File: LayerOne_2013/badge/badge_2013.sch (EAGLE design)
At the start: 122 parts, among them CON2 EXT, CON6 J8, CON8 J3, IC1 SLICE_NOSHIFT_TLC5947HTSSOP32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, IC3 SLICE_NOSHIFT_TLC5947HTSSOP32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, IC4 TL064D, K1 5-XX, K2 5-XX, K3 5-XX, K4 5-XX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

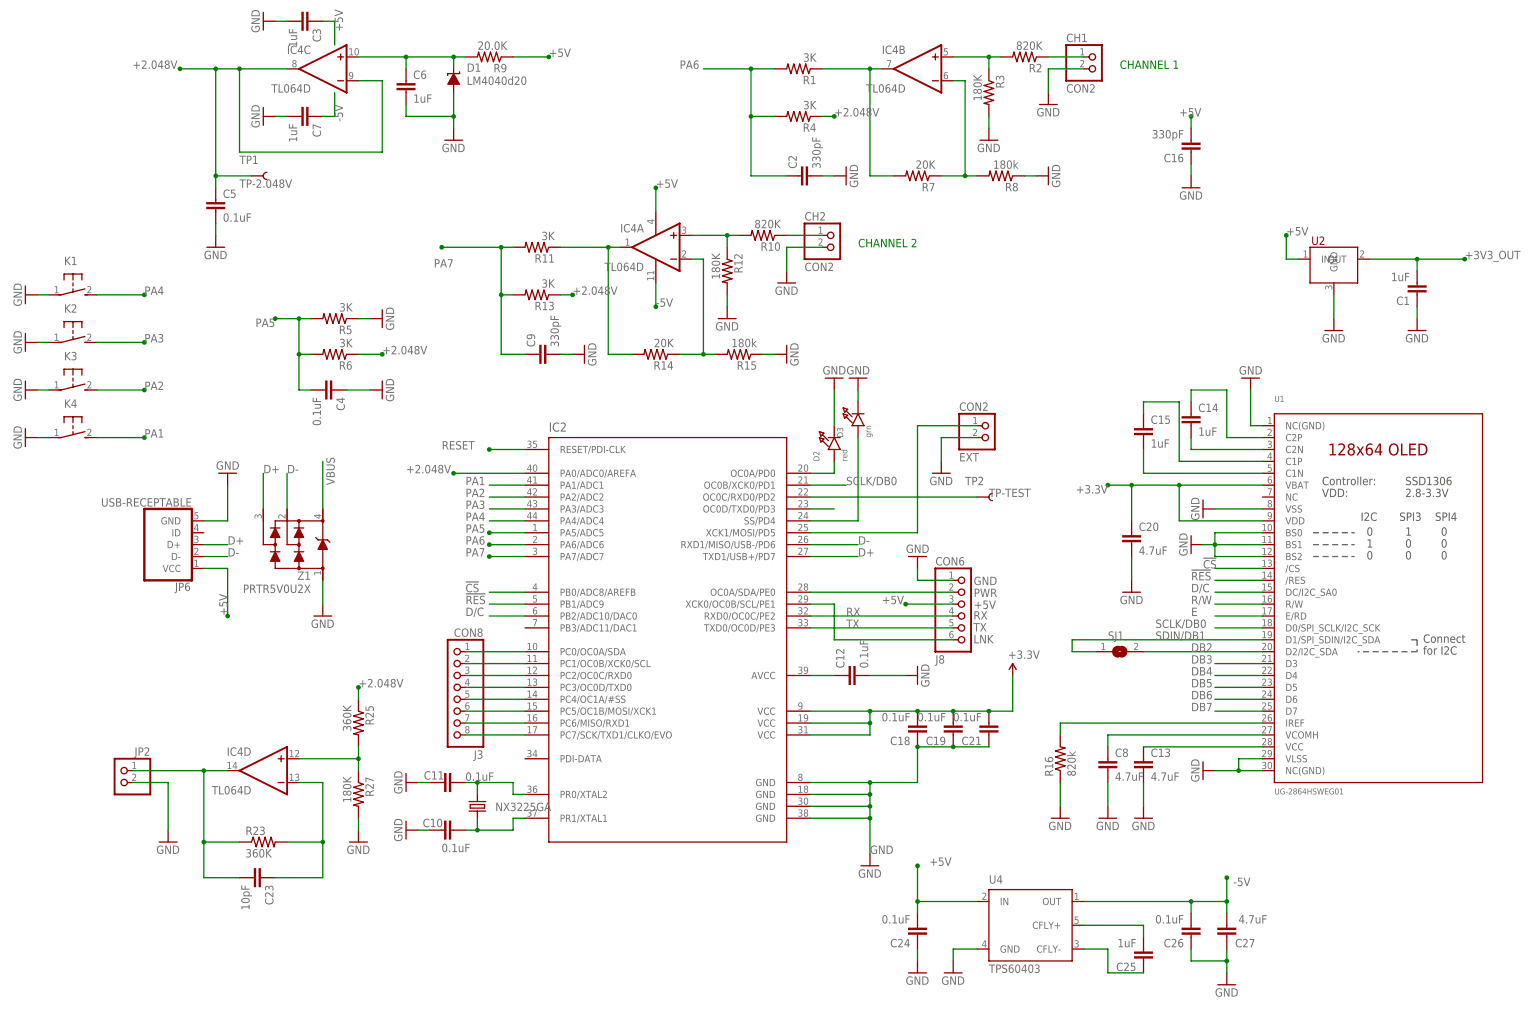
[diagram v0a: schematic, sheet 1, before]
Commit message: 
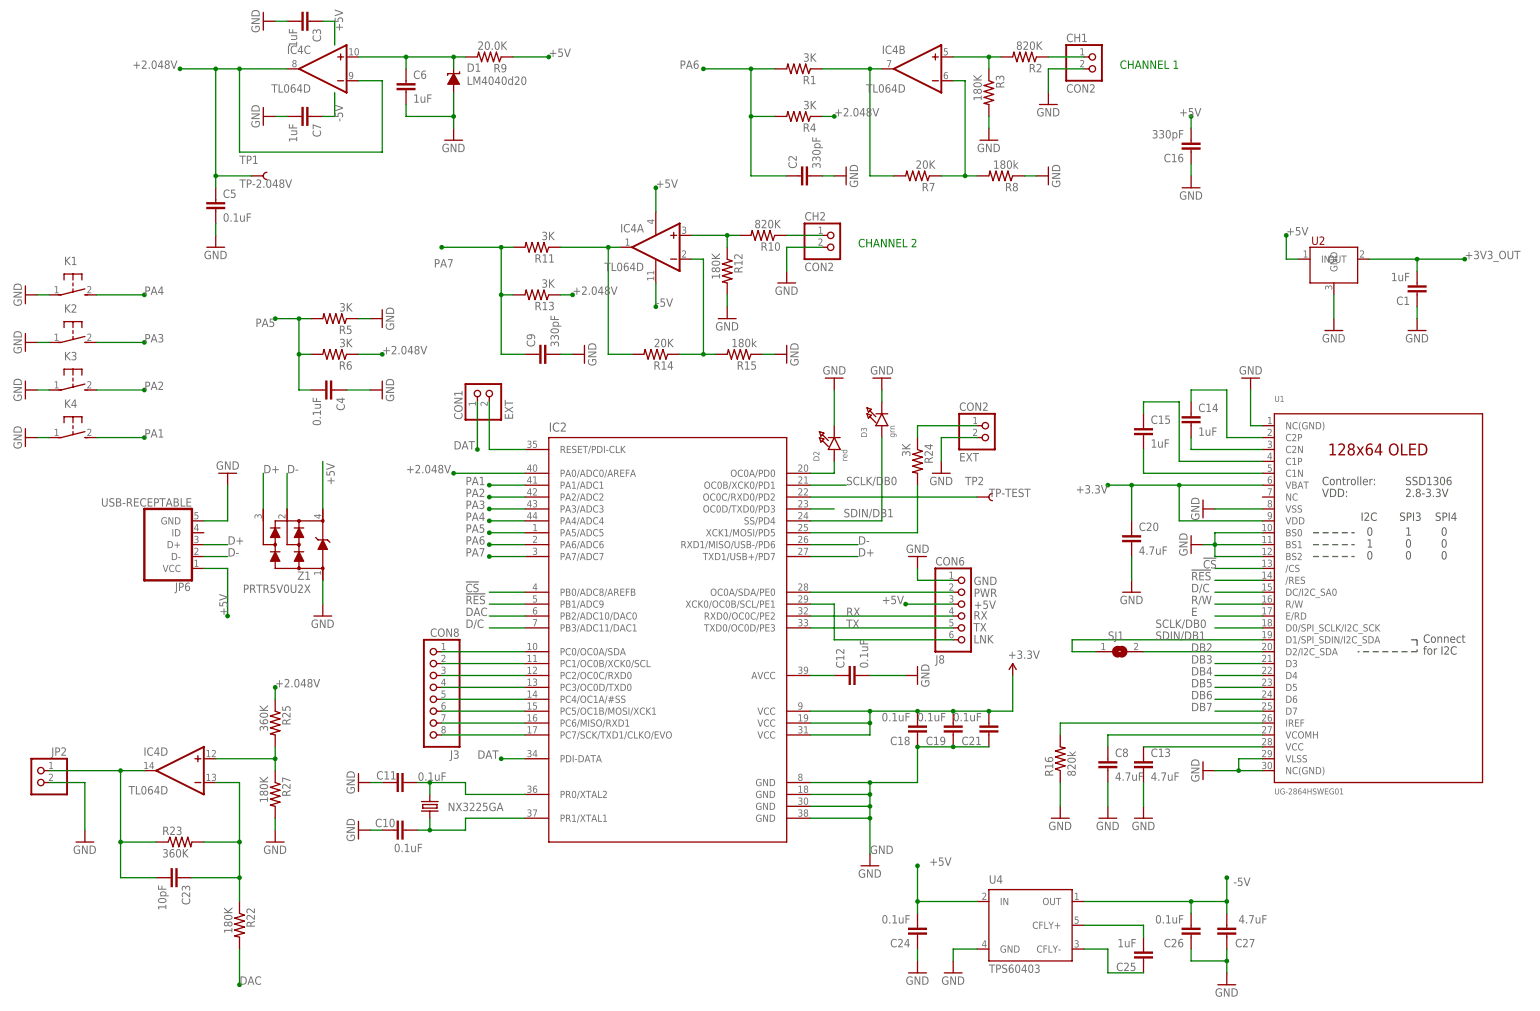
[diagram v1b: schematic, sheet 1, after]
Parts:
- added CON1: EXT, microbuilder:HEADER-1X2
- added R22: 180K, resistor:R-US_R0805
- added R24: 3K, resistor:R-US_R0805
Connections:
- removed net RESET: IC2.RESET/PDI-CLK
- removed net VBUS: Z1.P$4
- new net DAC: IC2.PB2/ADC10/DAC0, R22.2
- new net DAT: CON1.1, IC2.PDI-DATA
- new net N$38: CON1.2, IC2.RESET/PDI-CLK
- new net N$6: CON2.1, R24.1
- net +5V: now also Z1.P$4
- net D/C: now also IC2.PB3/ADC11/DAC1; no longer IC2.PB2/ADC10/DAC0
- net N$19: now also R24.2; no longer CON2.1
- net N$24: now also R22.1
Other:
- moved on the sheet: C10, C11, C23, CON8, D3, IC4D, JP2, R23, R25, R27

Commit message: 
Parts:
- PDI: value EXT -> CON6
- renumbered CON1 to PDI
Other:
- moved on the sheet: C4, K1, K2, K3, K4, R5, R6

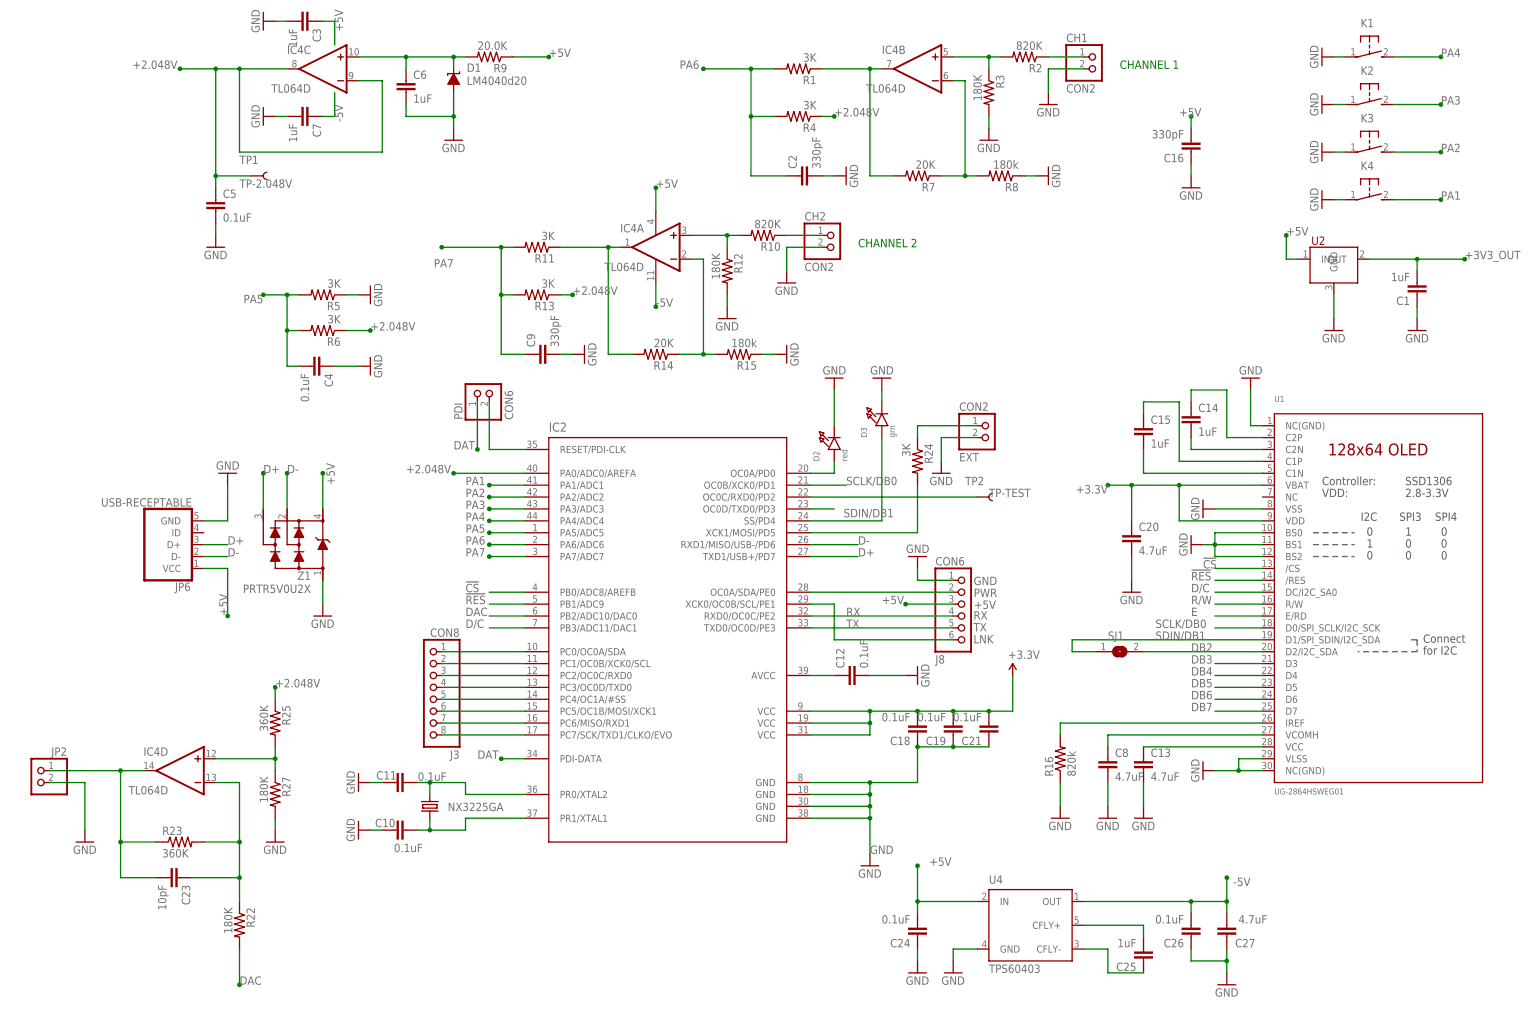
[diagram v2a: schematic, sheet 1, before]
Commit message: 
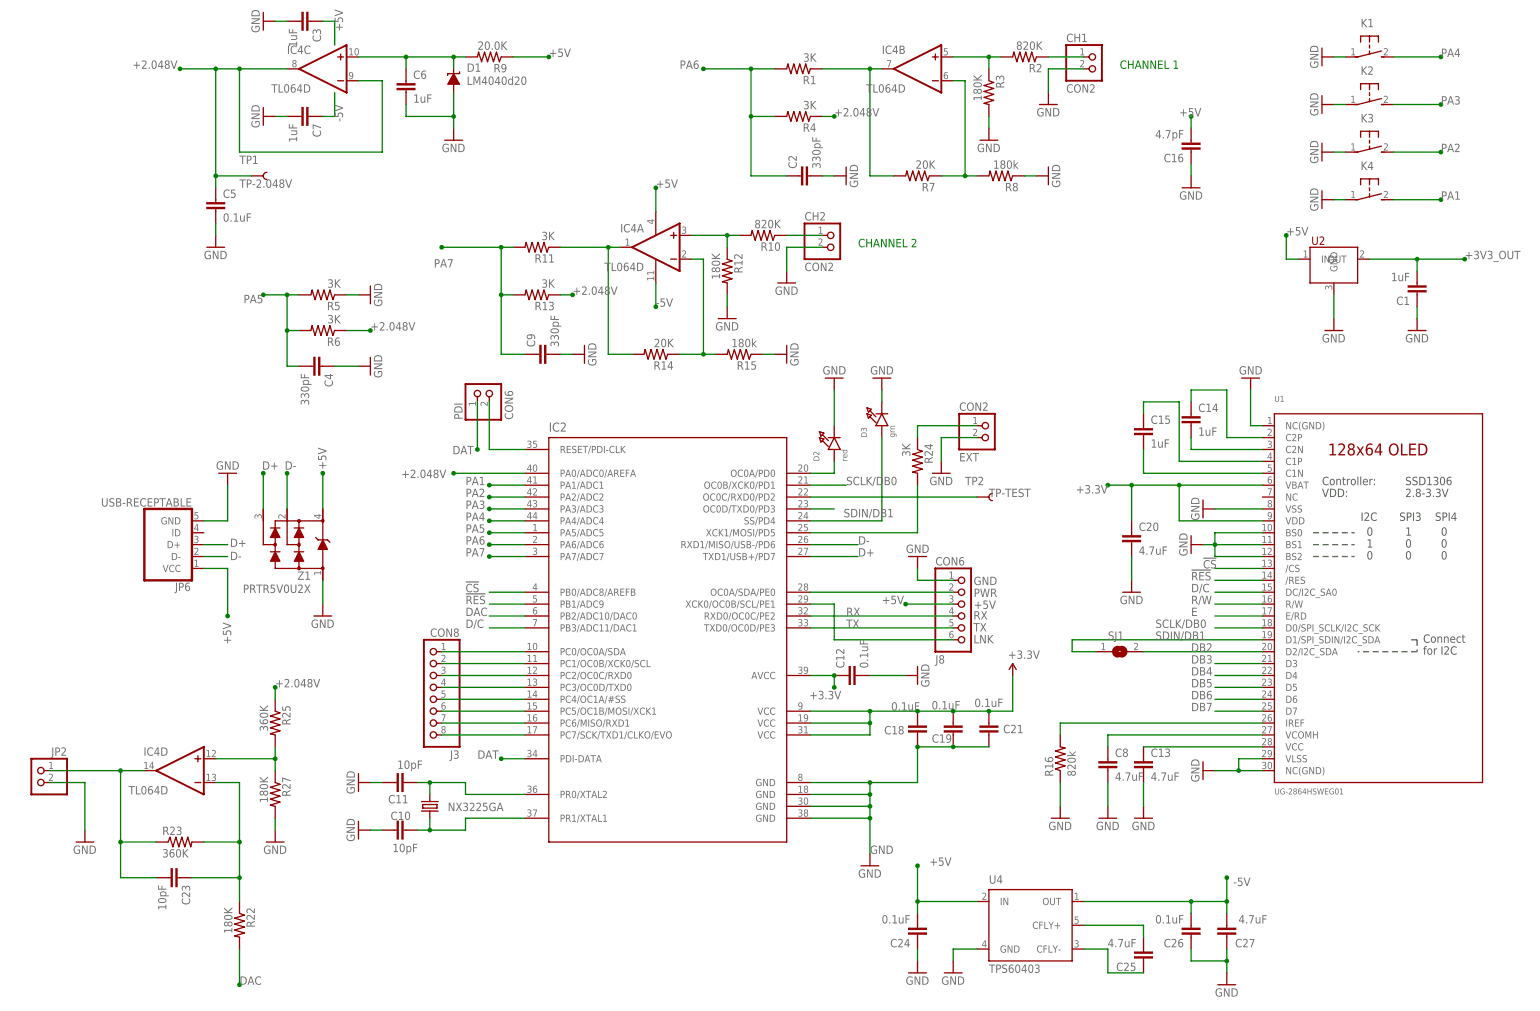
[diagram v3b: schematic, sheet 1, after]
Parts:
- C10, C11: value 0.1uF -> 10pF
- C16: value 330pF -> 4.7pF
- C25: value 1uF -> 4.7uF
- C4: value 0.1uF -> 330pF
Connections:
- removed net N$15: C12.1, IC2.AVCC
- net +3.3V: now also C12.1, IC2.AVCC
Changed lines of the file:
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@@
 <part name="C1" library="SparkFun" deviceset="CAP" device="0805" value="1uF"/>
 <part name="C3" library="SparkFun" deviceset="CAP" device="0805" value="1uF"/>
-<part name="C4" library="SparkFun" deviceset="CAP" device="0805" value="0.1uF"/>
+<part name="C4" library="SparkFun" deviceset="CAP" device="0805" value="330pF"/>
 <part name="JP2" library="microbuilder" deviceset="HEADER-1X2" device=""/>
 <part name="CH1" library="microbuilder" deviceset="HEADER-1X2" device="" value="CON2"/>
@@
 <part name="GND25" library="SparkFun" deviceset="GND" device=""/>
 <part name="GND26" library="SparkFun" deviceset="GND" device=""/>
-<part name="C16" library="SparkFun" deviceset="CAP" device="0805" value="330pF"/>
+<part name="C16" library="SparkFun" deviceset="CAP" device="0805" value="4.7pF"/>
 <part name="CH2" library="microbuilder" deviceset="HEADER-1X2" device="" value="CON2"/>
 <part name="R10" library="resistor" deviceset="R-US_" device="R0805" value="820K"/>
@@
 <part name="GND35" library="SparkFun" deviceset="GND" device=""/>
 <part name="U4" library="RHD2000_eval_board" deviceset="TPS60403" device=""/>
-<part name="C25" library="SparkFun" deviceset="CAP" device="0805" value="1uF"/>
+<part name="C25" library="SparkFun" deviceset="CAP" device="0805" value="4.7uF"/>
 <part name="C24" library="SparkFun" deviceset="CAP" device="0805" value="0.1uF"/>
 <part name="GND36" library="SparkFun" deviceset="GND" device=""/>
@@
 <part name="GND41" library="SparkFun" deviceset="GND" device=""/>
 <part name="X2" library="M6-RF315" deviceset="NX3225GA" device=""/>
-<part name="C10" library="SparkFun" deviceset="CAP" device="0805" value="0.1uF"/>
-<part name="C11" library="SparkFun" deviceset="CAP" device="0805" value="0.1uF"/>
+<part name="C10" library="SparkFun" deviceset="CAP" device="0805" value="10pF"/>
+<part name="C11" library="SparkFun" deviceset="CAP" device="0805" value="10pF"/>
 <part name="GND42" library="SparkFun" deviceset="GND" device=""/>
 <part name="GND44" library="SparkFun" deviceset="GND" device=""/>
@@
 <instance part="GND5" gate="1" x="215.9" y="45.72"/>
 <instance part="CON8" gate="A" x="121.92" y="81.28" rot="MR0"/>
-<instance part="C18" gate="G$1" x="226.06" y="76.2" rot="R180"/>
-<instance part="C19" gate="G$1" x="233.68" y="76.2" rot="R180"/>
-<instance part="C21" gate="G$1" x="241.3" y="76.2" rot="R180"/>
+<instance part="C18" gate="G$1" x="226.06" y="76.2" smashed="yes" rot="R180">
+<attribute name="NAME" x="223.266" y="75.565" size="1.778" layer="95" rot="R180"/>
+<attribute name="VALUE" x="226.568" y="80.645" size="1.778" layer="96" rot="R180"/>
+</instance>
+<instance part="C19" gate="G$1" x="233.68" y="76.2" smashed="yes" rot="R180">
+<attribute name="NAME" x="233.426" y="73.787" size="1.778" layer="95" rot="R180"/>
+<attribute name="VALUE" x="235.204" y="80.899" size="1.778" layer="96" rot="R180"/>
+</instance>
+<instance part="C21" gate="G$1" x="241.3" y="76.2" smashed="yes" rot="R180">
+<attribute name="NAME" x="248.666" y="75.819" size="1.778" layer="95" rot="R180"/>
+<attribute name="VALUE" x="244.348" y="81.407" size="1.778" layer="96" rot="R180"/>
+</instance>
 <instance part="+3.3V" gate="1" x="246.38" y="86.36"/>
 <instance part="CON2" gate="G$1" x="241.3" y="137.16"/>
@@
 </instance>
 <instance part="C10" gate="G$1" x="116.84" y="53.34" smashed="yes" rot="R90">
-<attribute name="NAME" x="114.554" y="55.753" size="1.778" layer="95" rot="R180"/>
-<attribute name="VALUE" x="120.396" y="50.419" size="1.778" layer="96" rot="R180"/>
+<attribute name="NAME" x="117.856" y="57.277" size="1.778" layer="95" rot="R180"/>
+<attribute name="VALUE" x="119.38" y="50.419" size="1.778" layer="96" rot="R180"/>
 </instance>
 <instance part="C11" gate="G$1" x="116.84" y="63.5" smashed="yes" rot="R90">
-<attribute name="NAME" x="114.808" y="65.913" size="1.778" layer="95" rot="R180"/>
-<attribute name="VALUE" x="125.476" y="65.659" size="1.778" layer="96" rot="R180"/>
+<attribute name="NAME" x="117.348" y="60.833" size="1.778" layer="95" rot="R180"/>
+<attribute name="VALUE" x="120.396" y="68.199" size="1.778" layer="96" rot="R180"/>
 </instance>
 <instance part="GND42" gate="1" x="106.68" y="53.34" rot="R270"/>
@@
 <pinref part="+3.3V" gate="1" pin="VCC"/>
 </segment>
+<segment>
+<pinref part="IC2" gate="G$1" pin="AVCC"/>
+<pinref part="C12" gate="G$1" pin="1"/>
+<wire x1="208.28" y1="86.36" x2="203.2" y2="86.36" width="0.1524" layer="91"/>
+<wire x1="208.28" y1="86.36" x2="208.28" y2="83.82" width="0.1524" layer="91"/>
+<junction x="208.28" y="83.82"/>
+<junction x="208.28" y="86.36"/>
+<label x="202.946" y="81.28" size="1.778" layer="95"/>
+</segment>
 </net>
 <net name="PWR" class="0">
@@
 <wire x1="78.74" y1="109.22" x2="78.74" y2="99.06" width="0.1524" layer="91"/>
 <pinref part="JP6" gate="G$1" pin="VCC"/>
-<label x="78.74" y="99.06" size="1.778" layer="95" rot="R90"/>
+<label x="79.502" y="92.964" size="1.778" layer="95" rot="R90"/>
 <junction x="78.74" y="99.06"/>
 </segment>
@@
 <pinref part="Z1" gate="G$1" pin="P$4"/>
 <wire x1="99.06" y1="121.92" x2="99.06" y2="129.54" width="0.1524" layer="91"/>
-<label x="101.6" y="127" size="1.778" layer="95" rot="R90"/>
+<label x="99.822" y="130.302" size="1.778" layer="95" rot="R90"/>
 <junction x="99.06" y="129.54"/>
 </segment>
@@
 <pinref part="Z1" gate="G$1" pin="P$2"/>
 <wire x1="91.44" y1="121.92" x2="91.44" y2="129.54" width="0.1524" layer="91"/>
-<label x="91.44" y="129.54" size="1.778" layer="95"/>
+<label x="90.932" y="130.302" size="1.778" layer="95"/>
 <junction x="91.44" y="129.54"/>
 </segment>
@@
 <wire x1="73.66" y1="111.76" x2="78.74" y2="111.76" width="0.1524" layer="91"/>
 <pinref part="JP6" gate="G$1" pin="D-"/>
-<label x="78.74" y="111.76" size="1.778" layer="95"/>
+<label x="79.248" y="110.998" size="1.778" layer="95"/>
 </segment>
 <segment>
@@
 <pinref part="Z1" gate="G$1" pin="P$3"/>
 <wire x1="86.36" y1="121.92" x2="86.36" y2="129.54" width="0.1524" layer="91"/>
-<label x="86.36" y="129.54" size="1.778" layer="95"/>
+<label x="86.106" y="130.302" size="1.778" layer="95"/>
 <junction x="86.36" y="129.54"/>
 </segment>
@@
 <wire x1="73.66" y1="114.3" x2="78.74" y2="114.3" width="0.1524" layer="91"/>
 <pinref part="JP6" gate="G$1" pin="D+"/>
-<label x="78.74" y="114.3" size="1.778" layer="95"/>
+<label x="79.248" y="113.792" size="1.778" layer="95"/>
 </segment>
 <segment>
@@
 <wire x1="218.44" y1="137.16" x2="218.44" y2="119.38" width="0.1524" layer="91"/>
 <wire x1="218.44" y1="119.38" x2="203.2" y2="119.38" width="0.1524" layer="91"/>
-</segment>
-</net>
-<net name="N$15" class="0">
-<segment>
-<pinref part="IC2" gate="G$1" pin="AVCC"/>
-<pinref part="C12" gate="G$1" pin="1"/>
-<wire x1="208.28" y1="86.36" x2="203.2" y2="86.36" width="0.1524" layer="91"/>
 </segment>
 </net>
@@
 <pinref part="IC2" gate="G$1" pin="PA0/ADC0/AREFA"/>
 <wire x1="142.24" y1="129.54" x2="127" y2="129.54" width="0.1524" layer="91"/>
-<label x="116.84" y="129.54" size="1.778" layer="95"/>
+<label x="115.824" y="128.524" size="1.778" layer="95"/>
 <junction x="127" y="129.54"/>
 </segment>
@@
 <wire x1="132.08" y1="144.78" x2="132.08" y2="134.62" width="0.1524" layer="91"/>
 <junction x="132.08" y="134.62"/>
-<label x="127" y="134.62" size="1.778" layer="95"/>
-</segment>
-<segment>
+<label x="126.746" y="133.604" size="1.778" layer="95"/>
+</segment>
+<segment>

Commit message: oled update
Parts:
- SJ1: device microbuilder:SOLDERJUMPERREFLOW_NOPASTE -> microbuilder:SOLDERJUMPERREFLOW
- U1: device microbuilder:DISP_OLED_UG-2864HSWEG010.96" -> badge.lbrbadge_2013:MICROBUILDER_DISP_OLED_UG-2864HSWEG010.96"
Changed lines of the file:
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@@
 <part name="BAT1" library="tvbgone-adj" deviceset="BATTERY" device="CR123A" value="CR123A"/>
 <part name="GND6" library="supply1" deviceset="GND" device=""/>
-<part name="U1" library="microbuilder" deviceset="DISP_OLED_UG-2864HSWEG01" device="0.96&quot;" value="UG-2864HSWEG01"/>
+<part name="U1" library="badge.lbrbadge_2013" deviceset="MICROBUILDER_DISP_OLED_UG-2864HSWEG01" device="0.96&quot;" value="UG-2864HSWEG01"/>
 <part name="C14" library="SparkFun" deviceset="CAP" device="0805" value="1uF"/>
 <part name="GND3" library="SparkFun" deviceset="GND" device=""/>
@@
 <part name="GND47" library="SparkFun" deviceset="GND" device=""/>
 <part name="JP1" library="microbuilder" deviceset="JUMPER3" device=""/>
-<part name="SJ1" library="microbuilder" deviceset="SOLDERJUMPER" device="REFLOW_NOPASTE"/>
+<part name="SJ1" library="microbuilder" deviceset="SOLDERJUMPER" device="REFLOW"/>
 <part name="R24" library="resistor" deviceset="R-US_" device="R0805" value="3K"/>
 <part name="PDI" library="microbuilder" deviceset="HEADER-1X2" device="" value="CON6"/>
